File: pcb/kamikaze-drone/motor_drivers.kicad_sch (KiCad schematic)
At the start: 16 parts, among them M1 Brushless DC, M2 Brushless DC, M3 Brushless DC, M4 Brushless DC, Q1 SI2300DS, Q2 SI2300DS, Q3 SI2300DS, Q4 SI2300DS

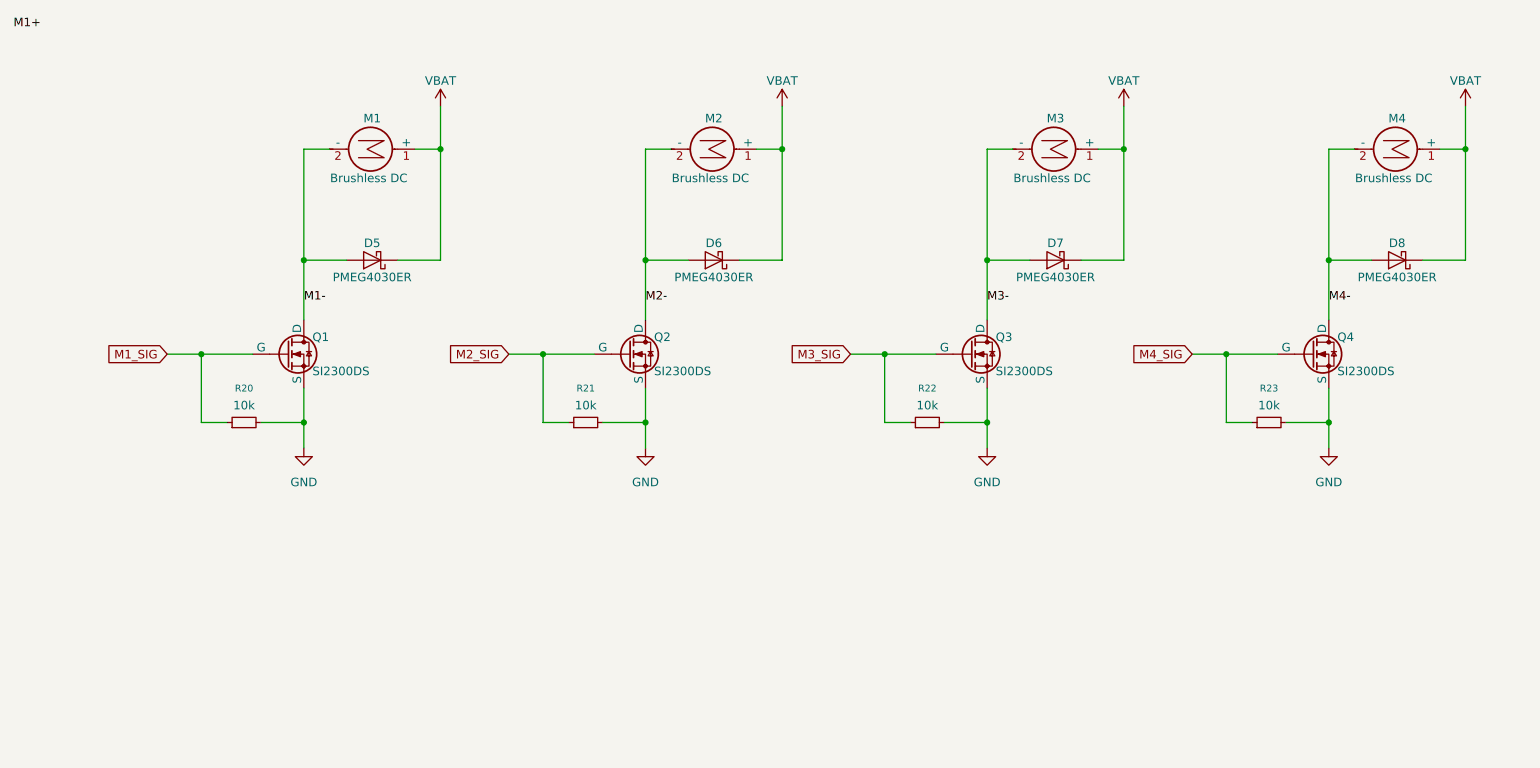
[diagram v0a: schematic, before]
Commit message: v2.0 of PCB completed
Updated routing to have USB port in center of top.
Shrank overall size to 50x50 mm
Layout is now ground+signal >> ground >> 3V3 >> signal

TODO: Add stitching vias between ground on top and second layer?
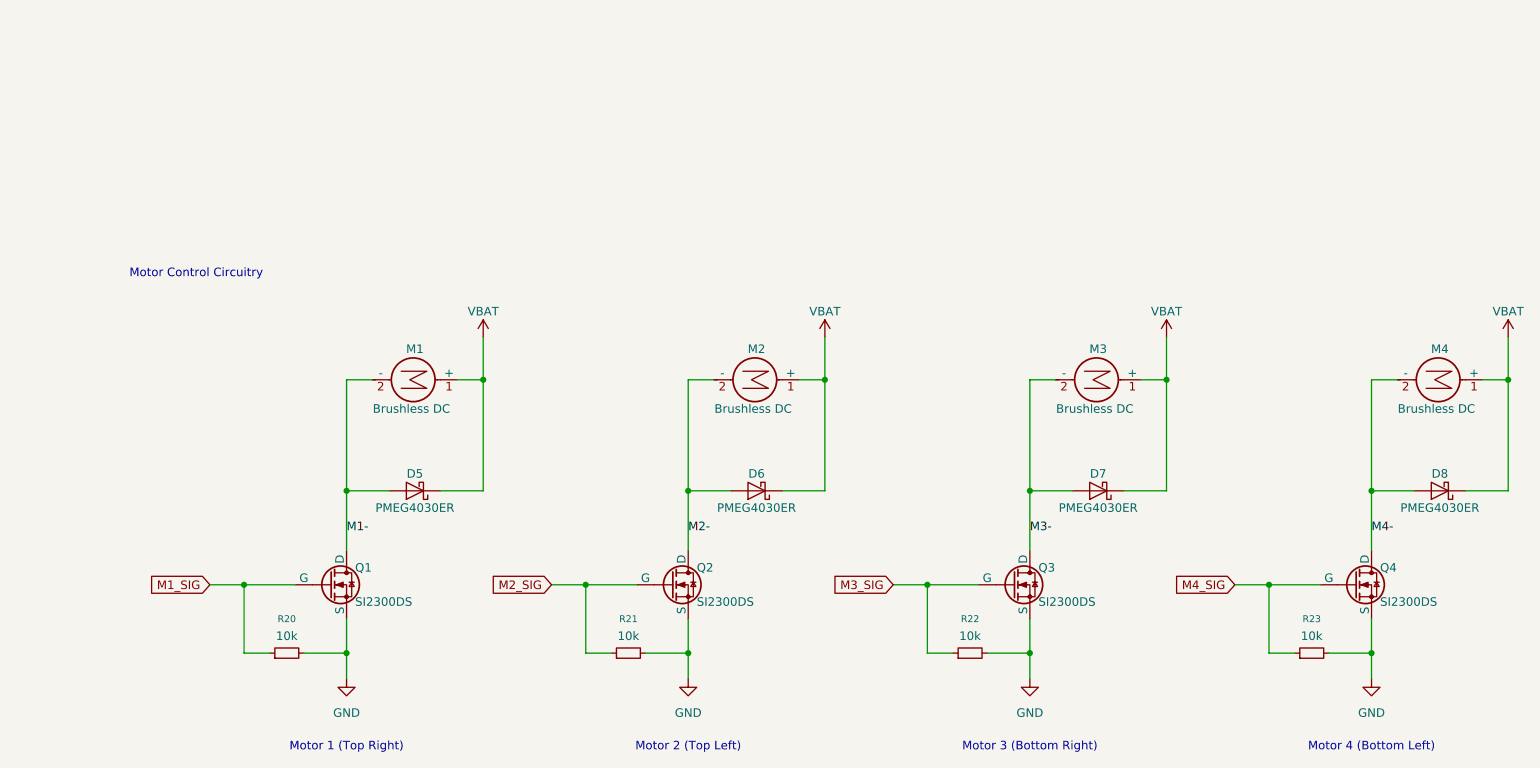
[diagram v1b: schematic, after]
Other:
- note added: "Motor 1 (Top Right)"
- note added: "Motor 2 (Top Left)"
- note added: "Motor 3 (Bottom Right)"
- note added: "Motor 4 (Bottom Left)"
- note added: "Motor Control Circuitry"
- moved on the sheet: D5, D6, D7, D8, M1, M2, M3, M4, Q1, Q2, Q3, Q4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

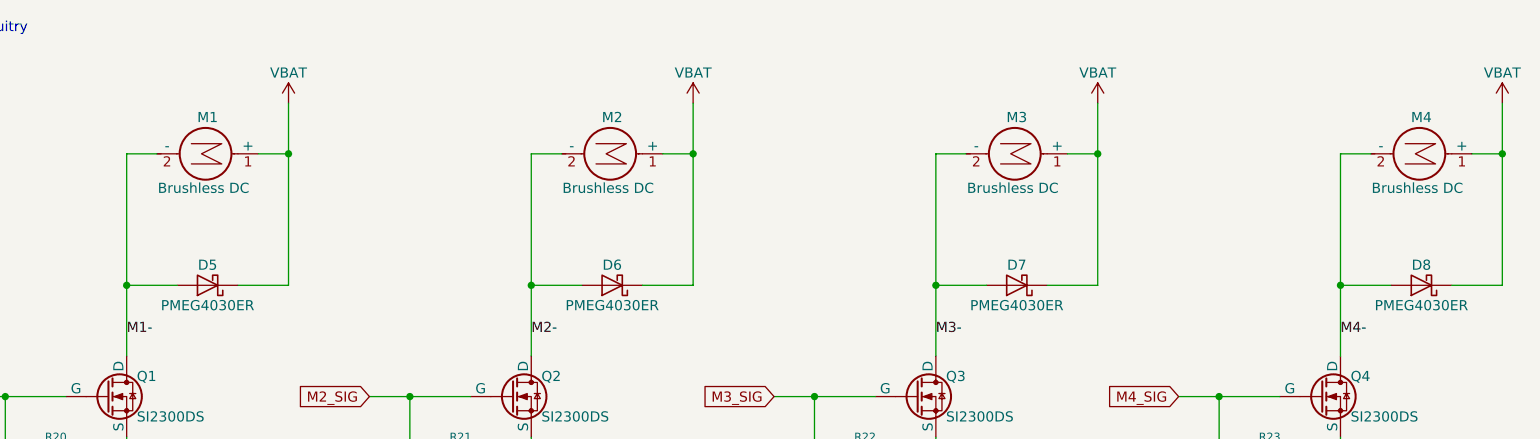
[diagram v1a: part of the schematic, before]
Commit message: v3 of PCB made. ov7670 implementation guide added
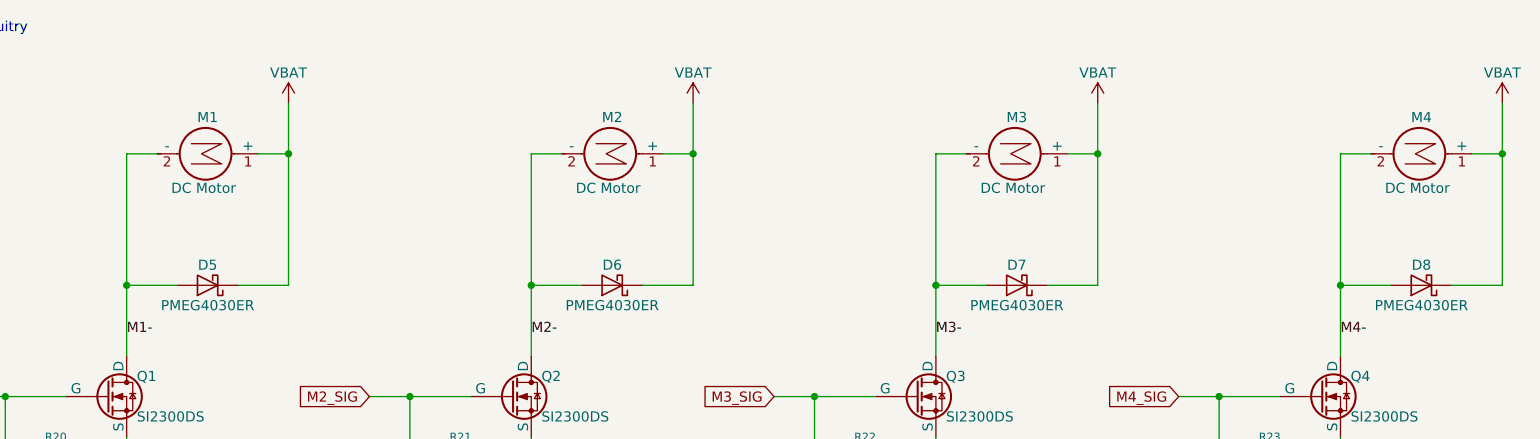
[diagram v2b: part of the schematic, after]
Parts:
- M1, M2, M3, M4: value Brushless DC -> DC Motor
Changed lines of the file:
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@@
 			)
 		)
-		(property "Value" "Brushless DC"
+		(property "Value" "DC Motor"
 			(at 234.442 84.328 90)
 			(effects
@@
 			)
 		)
-		(property "Value" "Brushless DC"
+		(property "Value" "DC Motor"
 			(at 183.642 84.328 90)
 			(effects
@@
 			)
 		)
-		(property "Value" "Brushless DC"
+		(property "Value" "DC Motor"
 			(at 132.842 84.328 90)
 			(effects
@@
 			)
 		)
-		(property "Value" "Brushless DC"
+		(property "Value" "DC Motor"
 			(at 82.042 84.328 90)
 			(effects
